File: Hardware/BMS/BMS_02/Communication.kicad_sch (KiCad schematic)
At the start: 43 parts, among them U13 ADUM1281ARZ-RL7, U14 ADUM1281ARZ-RL7, U7 FT230XS, U8 MCP2562-E-SN

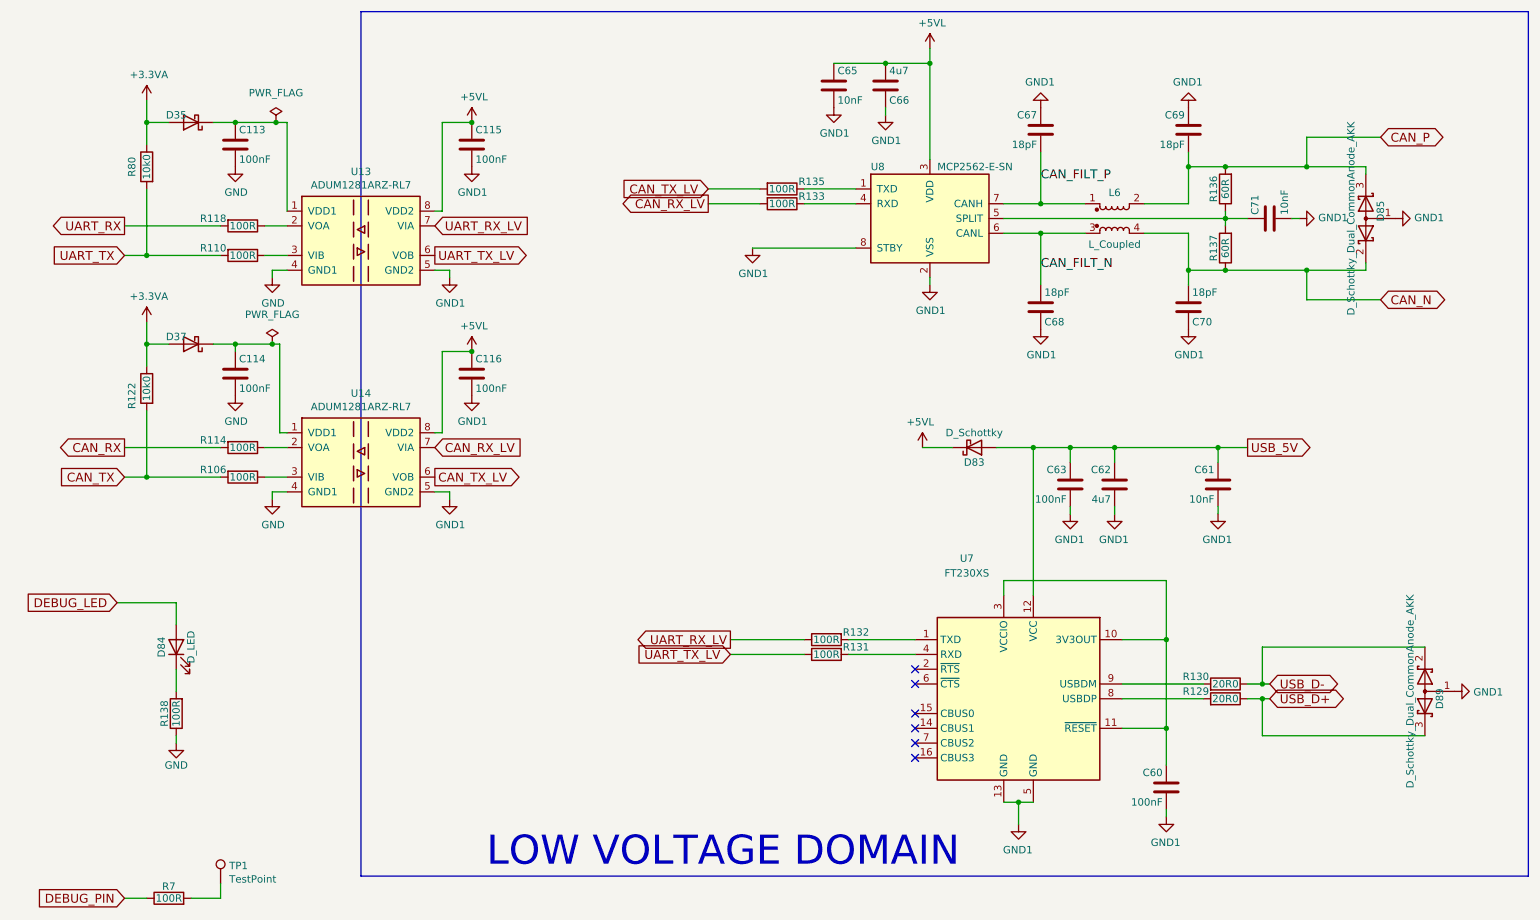
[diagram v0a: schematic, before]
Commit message: bms 02 build and code bring up. Board is built, bootloader is stable and uploads app flawlessly.
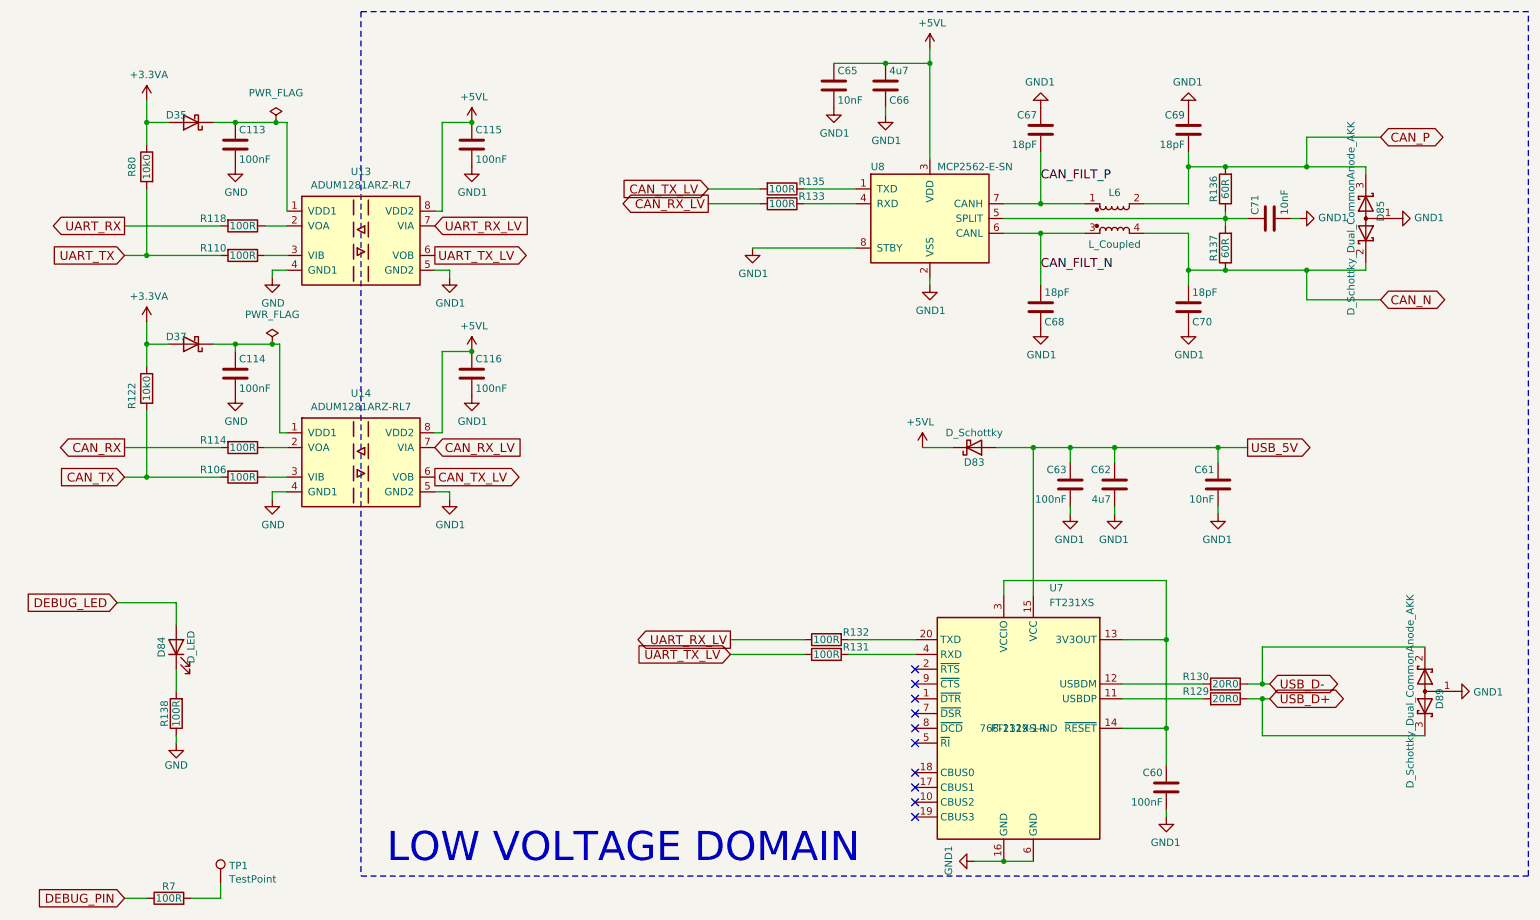
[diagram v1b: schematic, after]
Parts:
- removed U7: FT230XS, Package_SO:SSOP-16_3.9x4.9mm_P0.635mm, symbol Interface_USB:FT230XS
- added U7: FT231XS, Package_SO:SSOP-20_3.9x8.7mm_P0.635mm, symbol Interface_USB:FT231XS
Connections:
- net GND1: now also U7.16 (GND), U7.6 (GND)
- net USB_5V: now also U7.15 (VCC)
- net at C60.1: now also U7.13 (3V3OUT), U7.14 (~{RESET}), U7.3 (VCCIO)
- net at R130.2: now also U7.12 (USBDM)
- net at R129.2: now also U7.11 (USBDP)
- net at R132.2: now also U7.20 (TXD)
- net at R131.2: now also U7.4 (RXD)
- no-connect marks 6 -> 10
